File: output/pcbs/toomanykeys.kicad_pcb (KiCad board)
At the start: 2 copper layers, 20.8 x 71.8 mm, 67 parts

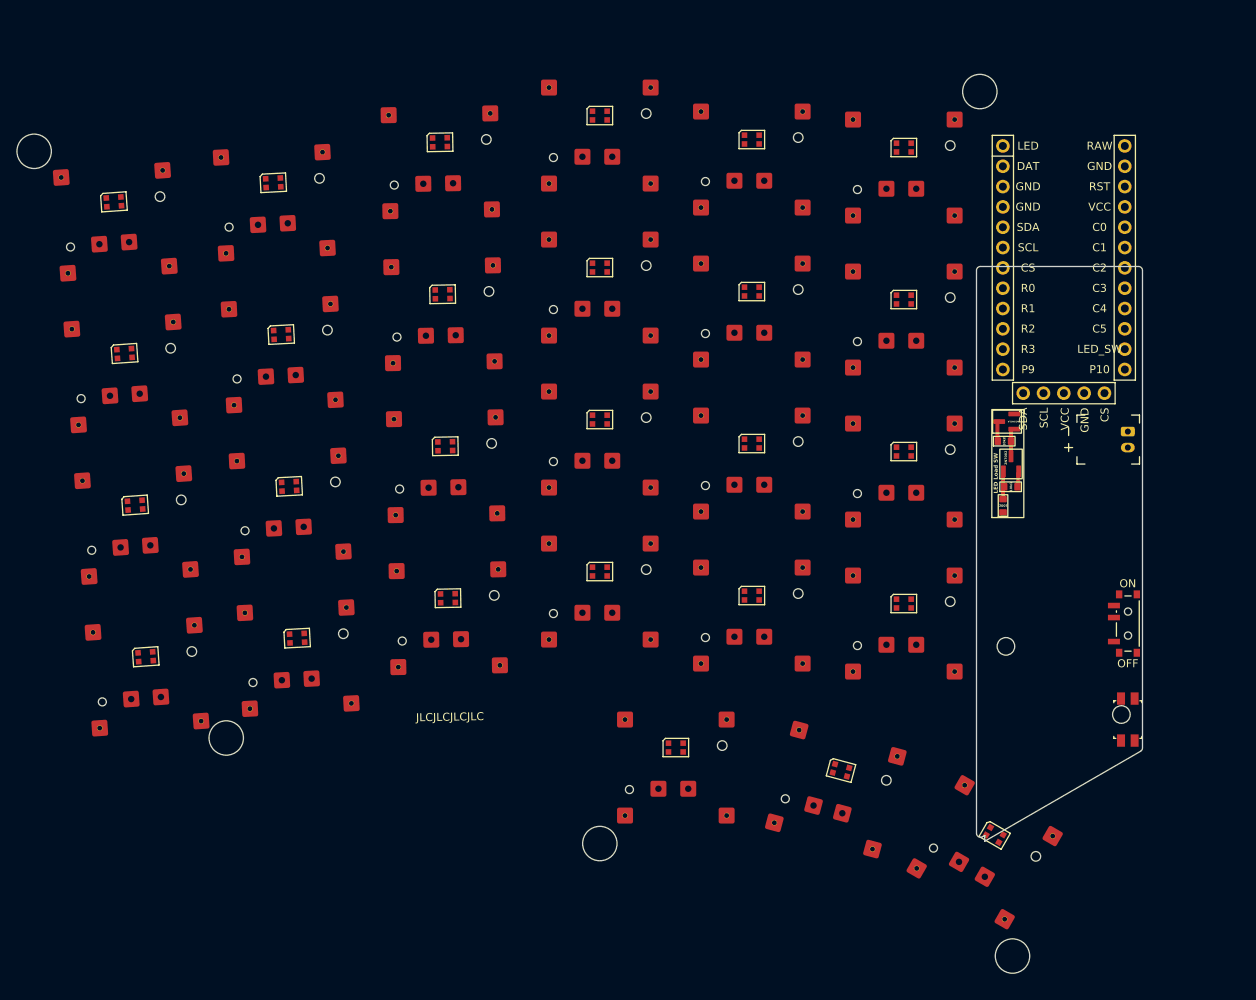
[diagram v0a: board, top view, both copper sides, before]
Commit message: Add BAV70 field and rotary, work on outlines.
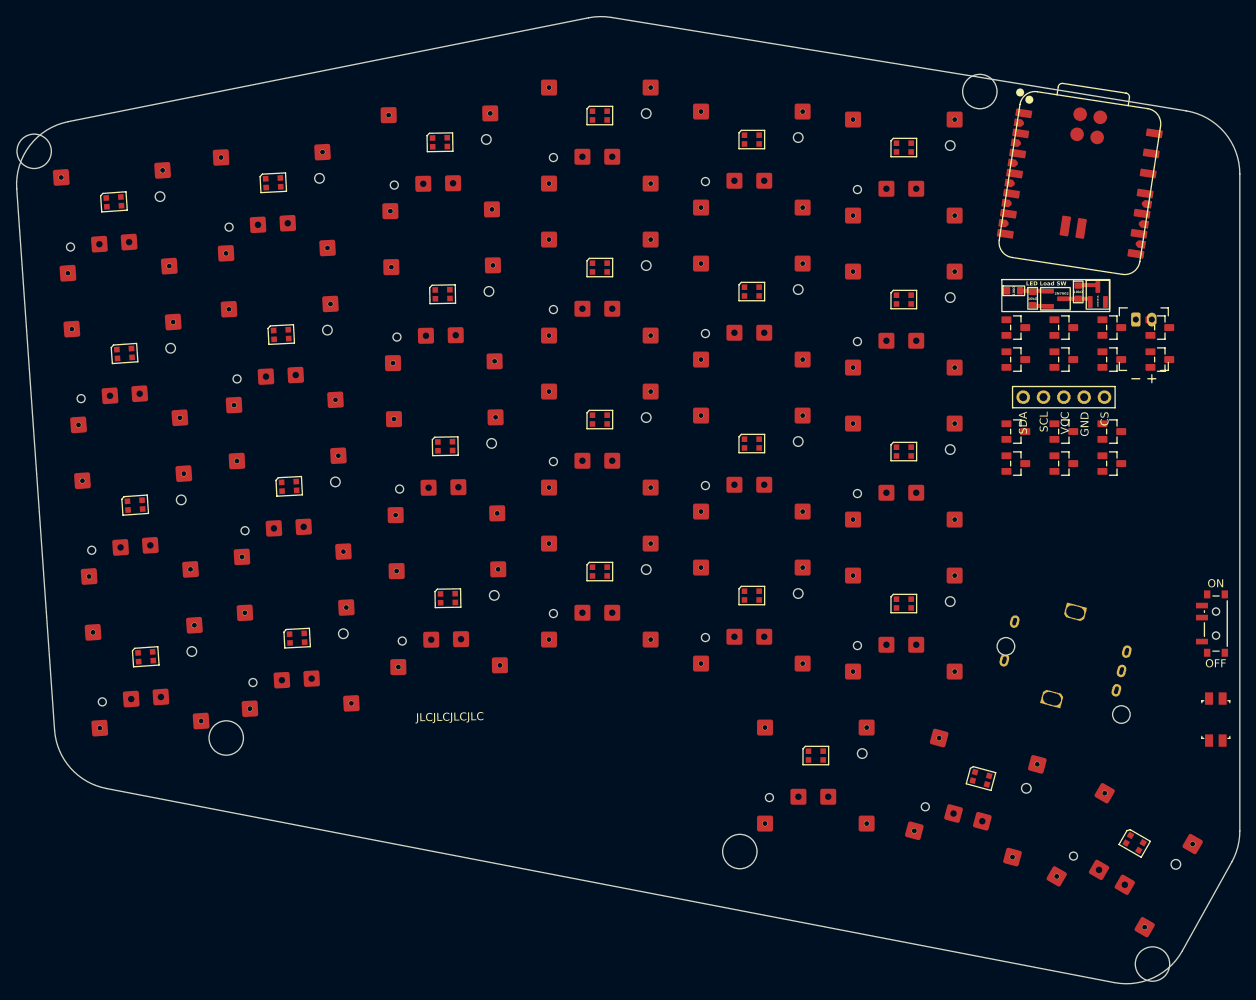
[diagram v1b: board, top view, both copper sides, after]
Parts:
- added D1: BAV70, BAV70 SOT23, F.Cu at (168.6, 116.4)
- added D10: BAV70, BAV70 SOT23, F.Cu at (168.6, 133.4)
- added D11: BAV70, BAV70 SOT23, F.Cu at (174.6, 133.4)
- added D12: BAV70, BAV70 SOT23, F.Cu at (180.6, 133.4)
- added D13: BAV70, BAV70 SOT23, F.Cu at (186.6, 116.4)
- added D14: BAV70, BAV70 SOT23, F.Cu at (186.6, 120.4)
- added D2: BAV70, BAV70 SOT23, F.Cu at (174.6, 116.4)
- added D3: BAV70, BAV70 SOT23, F.Cu at (180.6, 116.4)
- added D4: BAV70, BAV70 SOT23, F.Cu at (168.6, 120.4)
- added D5: BAV70, BAV70 SOT23, F.Cu at (174.6, 120.4)
- added D6: BAV70, BAV70 SOT23, F.Cu at (180.6, 120.4)
- added D7: BAV70, BAV70 SOT23, F.Cu at (168.6, 129.4)
- added D8: BAV70, BAV70 SOT23, F.Cu at (174.6, 129.4)
- added D9: BAV70, BAV70 SOT23, F.Cu at (180.6, 129.4)
- added RE1: , ceoloide:rotary_encoder_ec11_ec12, F.Cu at (174.6, 157.3)
- MCU1: footprint ceoloide:mcu_nice_nano -> XIAO-nRF52840-Plus-SMD
- moved XX1 21.8 mm to (173.6, 112.4), turned to 0 degrees
- moved LED27 17.5 mm to (183.5, 180.8)
- moved MH7 17.5 mm to (185.7, 195.9)
- moved S27 17.5 mm to (182.2, 182.9)
- moved LED25 17.5 mm to (143.6, 169.9)
- moved LED26 17.5 mm to (164.2, 172.7)
- moved MH6 17.5 mm to (134.1, 181.9)
- moved S25 17.5 mm to (143.6, 172.4)
- moved S26 17.5 mm to (163.6, 175.1)
- moved JST1 15.1 mm to (184.6, 115.4), turned to 0 degrees
- moved PWR1 11.0 mm to (193.6, 153.4)
- moved RST1 11.0 mm to (193.6, 165.4)
- moved MCU1 8.25 mm to (176.6, 98.4), turned to 81.3 degrees
- moved DISP1 0.50 mm to (174.6, 108.4)
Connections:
- net DAT renamed P1.07
- net LED renamed DIO
- net P10 renamed 3V3
- net R0 renamed P1.01
- net R1 renamed P0.19
- net R2 renamed P0.15
- net far_fan renamed thumb_far_fan
- net index_bottom renamed finger_index_bottom
- net index_home renamed finger_index_home
- net index_num renamed finger_index_num
- net index_top renamed finger_index_top
- net inner_bottom renamed finger_inner_bottom
- net inner_home renamed finger_inner_home
- net inner_num renamed finger_inner_num
- net inner_top renamed finger_inner_top
- net mid_fan renamed thumb_mid_fan
- net middle_bottom renamed finger_middle_bottom
- net middle_home renamed finger_middle_home
- net middle_num renamed finger_middle_num
- net middle_top renamed finger_middle_top
- net near_fan renamed thumb_near_fan
- net outer_bottom renamed finger_outer_bottom
- net outer_home renamed finger_outer_home
- net outer_num renamed finger_outer_num
- net outer_top renamed finger_outer_top
- net pinky_bottom renamed finger_pinky_bottom
- net pinky_home renamed finger_pinky_home
- net pinky_num renamed finger_pinky_num
- net pinky_top renamed finger_pinky_top
- net ring_bottom renamed finger_ring_bottom
- net ring_home renamed finger_ring_home
- net ring_num renamed finger_ring_num
- net ring_top renamed finger_ring_top
- MCU1 pad 1: RAW -> P0.02
- MCU1 pad 10: C5 -> P1.14
- MCU1 pad 11: LED_SW -> P1.15
- MCU1 pad 13: P9 -> GND
- MCU1 pad 14: R3 -> 5V
- MCU1 pad 18: CS -> P0.09
- MCU1 pad 19: SCL -> P0.10
- MCU1 pad 2: GND -> P0.03
- MCU1 pad 20: SDA -> P0.31
- MCU1 pad 21: GND -> P1.03
- MCU1 pad 22: GND -> P1.05
- MCU1 pad 3: RST -> P0.28
- MCU1 pad 4: VCC -> P0.29
- MCU1 pad 5: C0 -> P0.04
- MCU1 pad 6: C1 -> P0.05
- MCU1 pad 7: C2 -> P1.11
- MCU1 pad 8: C3 -> P1.12
- MCU1 pad 9: C4 -> P1.13
- S25 pad 1: C3 -> C2
- S26 pad 1: C4 -> C3
- S27 pad 1: C5 -> C4
- XX1 pad 2: RAW -> 5V
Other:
- board size 20.8 x 71.8 mm -> 152.9 x 120.9 mm
